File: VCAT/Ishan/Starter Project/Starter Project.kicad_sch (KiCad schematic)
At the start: 41 parts, among them J1 USB_C_Receptacle_USB2.0_16P, J2 Conn_01x04, J3 TC2030, J4 Conn_Coaxial, SW1 SW_Push, U1 MIC5365-3.3YD5, U2 USBLC6-2SC6, U3 STM32WB55CEU6, X1 32.768kHz, X2 32mHz

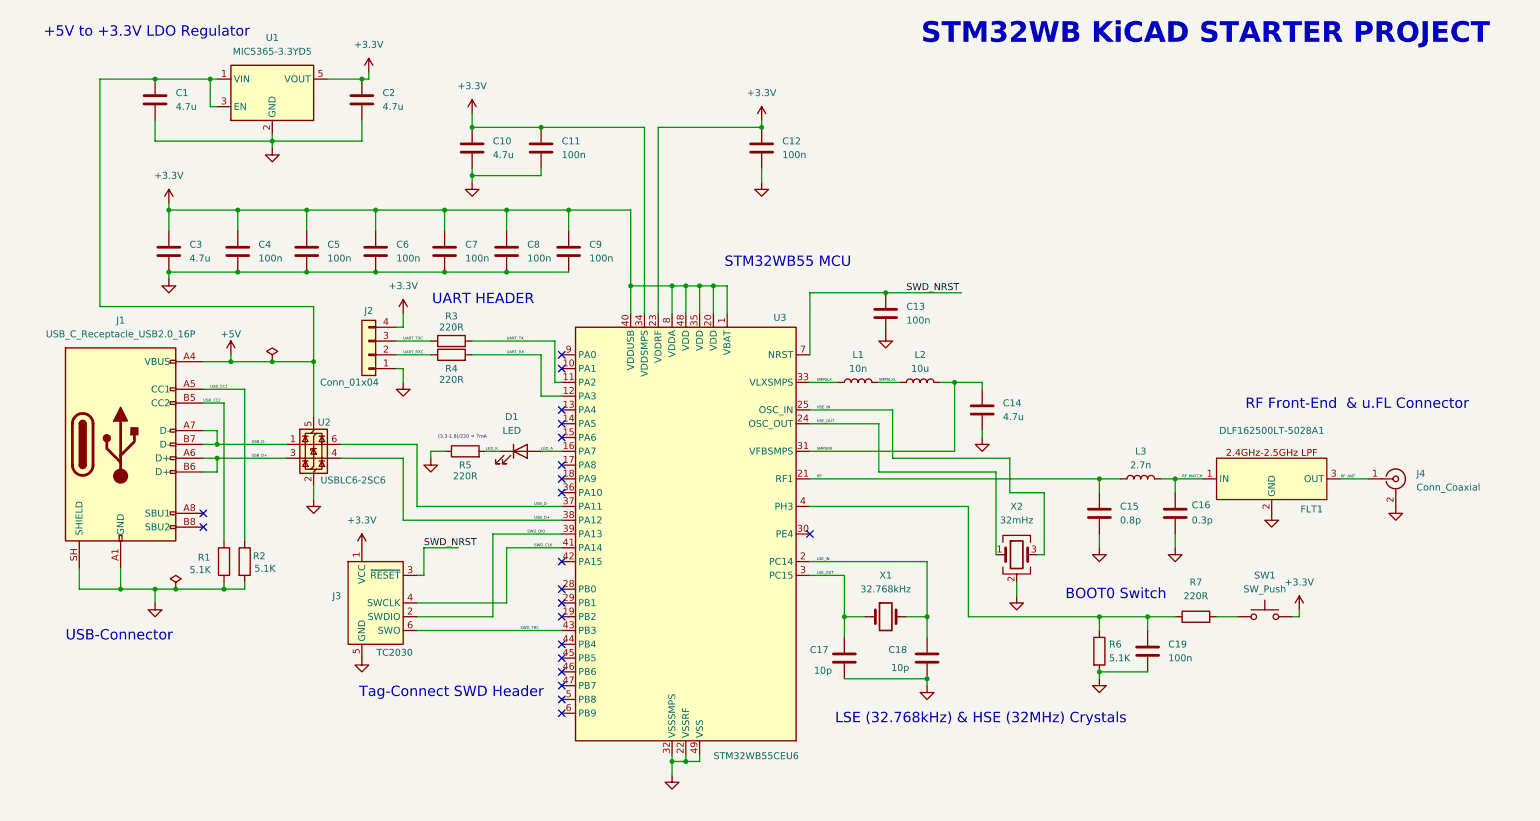
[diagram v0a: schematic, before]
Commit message: Everything is done
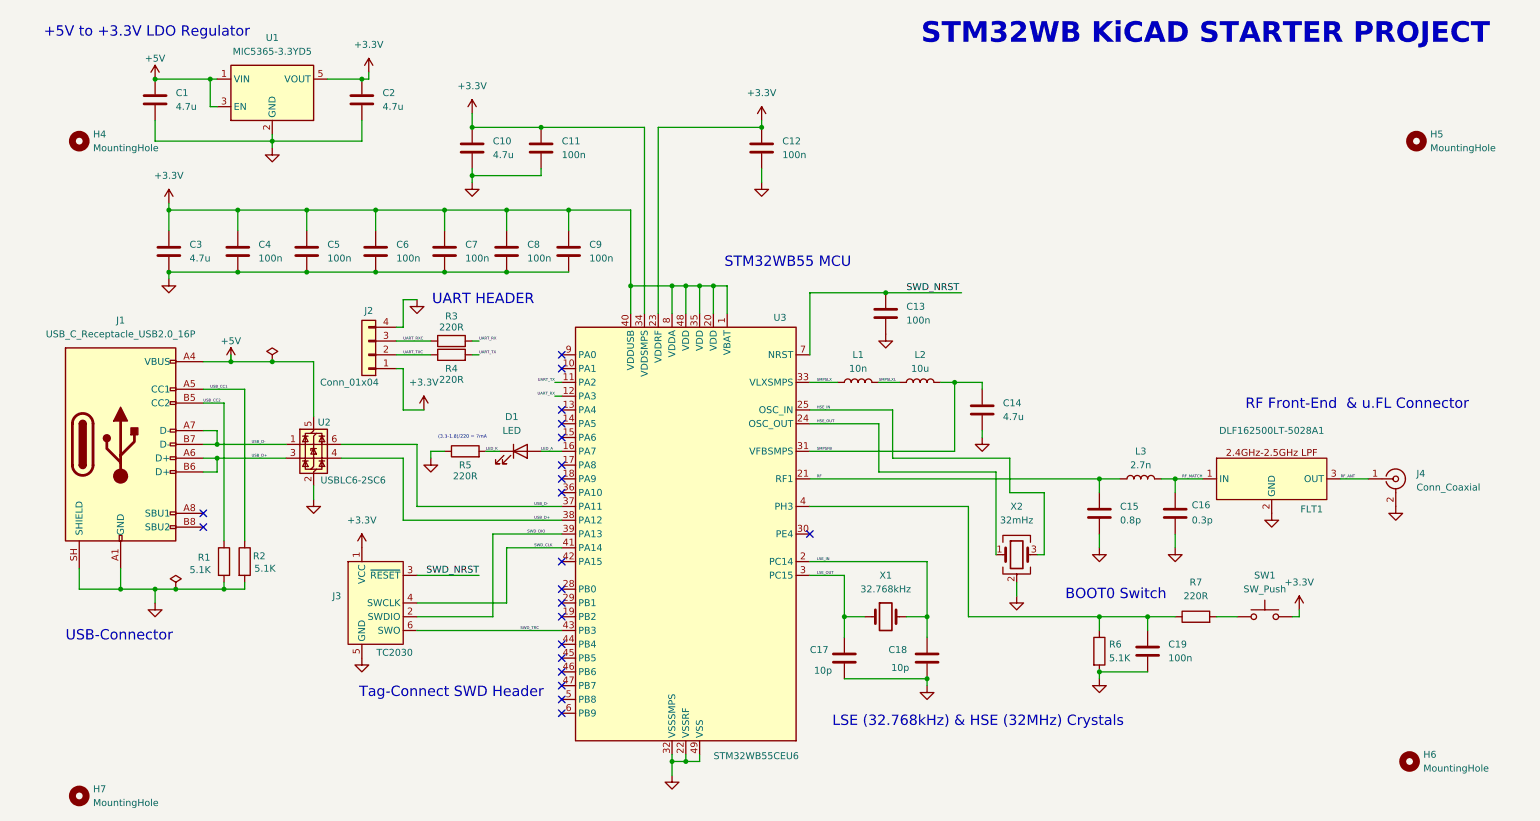
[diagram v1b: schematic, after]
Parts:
- added H4, H5, H6, H7: MountingHole, MountingHole:MountingHole_2.2mm_M2_ISO14580_Pad, symbol Mechanical:MountingHole
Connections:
- net +3.3V: now also J2.1 (Pin_1); no longer J2.4 (Pin_4)
- net GND: now also J2.4 (Pin_4); no longer J2.1 (Pin_1)
- net UART_RX: now also R3.2; no longer R4.2
- net UART_RXC: now also J2.3 (Pin_3), R3.1; no longer J2.2 (Pin_2), R4.1
- net UART_TX: now also R4.2; no longer R3.2
- net UART_TXC: now also J2.2 (Pin_2), R4.1; no longer J2.3 (Pin_3), R3.1
